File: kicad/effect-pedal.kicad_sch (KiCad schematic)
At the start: 83 parts, among them J1 NJ3FD-V, J10 USB_C_Receptacle_USB2.0_14P, J11 Conn_ST_STDC14, J2 NJ3FD-V, J3 Conn_01x08, J4 Conn_01x06, J5 Conn_01x06, J6 SOIC Bite Connector, J7 SOIC Bite Connector, J8 SOIC Bite Connector, J9 SOIC Bite Connector, Q1 NMOS, Q2 NMOS, SW1 RotaryEncoder_Switch, SW2 RotaryEncoder_Switch, SW3 RotaryEncoder_Switch, SW4 RotaryEncoder_Switch, SW5 SW_3PDT_x3, SW6 SW_SPDT, SW7 SW_Push, U1 STM32H723ZGTx, U2 PCM5102A, U3 USBLC6-2SC6, Y1 Crystal

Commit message: Finish part sourcing and start PCB layout
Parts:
- removed C27: 1u, Capacitor_SMD:C_0603_1608Metric, symbol Device:C
- removed C34: 10u, Capacitor_SMD:C_0603_1608Metric, symbol Device:C
- removed R3: 10k, Resistor_SMD:R_0603_1608Metric, symbol Device:R_US
- removed SW6: SW_SPDT, Button_Switch_SMD:SW_SPST_B3S-1100, symbol Switch:SW_SPDT
- removed TP5: TestPoint, TestPoint:TestPoint_Pad_2.0x2.0mm, symbol Connector:TestPoint
- added C28: 10u, Capacitor_SMD:C_0603_1608Metric, symbol Device:C
- added C33: 10n, Capacitor_SMD:C_0603_1608Metric, symbol Device:C
- added C8: 1u, Capacitor_SMD:C_0603_1608Metric, symbol Device:C
- added D3, D4: D_Schottky_Dual_Series_ACK_Split, Package_TO_SOT_SMD:TSOT-23, symbol Custom:D_Schottky_Dual_Series_ACK_Split_BAT
- added JP1: Jumper_2_Open, TestPoint:TestPoint_2Pads_Pitch2.54mm_Drill0.8mm, symbol Jumper:Jumper_2_Open
- added R1, R2: 1M, Resistor_SMD:R_0603_1608Metric, symbol Device:R_US
- added R15, R16: 100k, Resistor_SMD:R_0603_1608Metric, symbol Device:R_US
- added R17, R18: 100, Resistor_SMD:R_0603_1608Metric, symbol Device:R_US
- added R5: 10k, Resistor_SMD:R_0603_1608Metric, symbol Device:R_US
- J1, J2: value NJ3FD-V -> NJ6FD-H; symbol Connector_Audio:NJ3FD-V -> Connector_Audio:NJ6FD-V
- J10: footprint (none) -> Connector_USB:USB_C_Receptacle_GCT_USB4110; symbol Connector:USB_C_Receptacle_USB2.0_14P -> Connector:USB_C_Receptacle_USB2.0_16P; Part 2169900002 -> USB4110-GF-A
- J11: footprint Connector_TE-Connectivity:TE_MATE-N-LOK_1-770973-x_2x07_P4.14mm_Horizontal -> Connector_PinHeader_1.27mm:PinHeader_2x07_P1.27mm_Vertical_SMD; Part (none) -> FTSH-107-01-L-DV-K-A
- J3: footprint Connector_JST:JST_XH_S8B-XH-A_1x08_P2.50mm_Horizontal -> Connector_JST:JST_PH_S8B-PH-SM4-TB_1x08-1MP_P2.00mm_Horizontal; symbol Connector_Generic:Conn_01x08 -> Connector_Generic_MountingPin:Conn_01x08_MountingPin; Part Generic -> S8B-PH-SM4-TB
- J5: value Conn_01x06 -> Conn_01x09; footprint Connector_JST:JST_XH_S9B-XH-A_1x09_P2.50mm_Horizontal -> Connector_JST:JST_PH_S9B-PH-SM4-TB_1x09-1MP_P2.00mm_Horizontal; symbol Connector_Generic:Conn_01x09 -> Connector_Generic_MountingPin:Conn_01x09_MountingPin; Part Generic -> S9B-PH-SM4-TB
- J6, J7, J8, J9, TP1, TP2, TP3, TP4: now left out of the parts list
- R13: renamed from R11; value 3.3k -> 100k
- R14: renamed from R12; value 3.3k -> 100k
- SW1, SW2, SW3, SW4: footprint Rotary_Encoder:RotaryEncoder_Bourns_Vertical_PEC12R-3x17F-Sxxxx -> Bournes:RotaryEncoder_Bourns_Vertical_PEC12R-3x17F-Sxxxx; symbol Device:RotaryEncoder_Switch -> Device:RotaryEncoder_Switch_MP
- SW6: renamed from SW7; footprint Button_Switch_THT:SW_PUSH_6mm -> Button_Switch_SMD:SW_Push_1P1T_NO_E-Switch_TL3301NxxxxxG; Part (none) -> 1571563-6
- renumbered C9 to C10, C10 to C11, C11 to C12, C12 to C13, C13 to C14, C14 to C15, C15 to C16, C16 to C17, C17 to C18, C18 to C19, C22 to C20, C20 to C21, C19 to C22, C26 to C23, C21 to C24, C28 to C25, C23 to C26, C33 to C27, C25 to C29, C29 to C30, C30 to C31, C24 to C32, C31 to C34, C32 to C35, C8 to C9, JP1 to JP2, JP2 to JP3, JP3 to JP4, R9 to R10, R10 to R11, R8 to R12, R13 to R19, R14 to R20, R1 to R3, R2 to R4, R4 to R6, R5 to R7, R6 to R8, R7 to R9
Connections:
- net AUD_IN_L: now also C27.1; no longer U1.60 (PE9)
- net AUD_IN_L_AMP: no longer J6.3 (Pin_3)
- net AUD_IN_R: now also C28.1; no longer U1.46 (PB0)
- net AUD_IN_R_AMP: now also J6.7 (Pin_7); no longer J6.1 (Pin_1)
- net AUD_WET_R: now also R11.1; no longer R11.2
- net BOOT: now also JP1.2 (B), R5.1
- net DISPLAY_BL: now also J3.1 (Pin_1); no longer J3.8 (Pin_8)
- net DISPLAY_CS: now also J3.4 (Pin_4); no longer J3.5 (Pin_5)
- net DISPLAY_DATA: now also J3.6 (Pin_6); no longer J3.3 (Pin_3)
- net DISPLAY_DC: now also J3.3 (Pin_3); no longer J3.6 (Pin_6)
- net DISPLAY_RST: now also J3.2 (Pin_2); no longer J3.7 (Pin_7)
- net DISPLAY_SCK: now also J3.5 (Pin_5); no longer J3.4 (Pin_4)
- net GND: now also J1.S, J3.7 (Pin_7), J5.3 (Pin_3), R12.2, C33.1, C8.1, D3.1 (A), D4.1 (A), R1.2, R16.2, R2.2, R5.2; no longer J3.2 (Pin_2), R12.1
- net VCC: now also C30.1, C34.1, J3.8 (Pin_8), U1.6 (VBAT), JP1.1 (A); no longer C22.1, C24.1, C26.1, C29.1, J3.1 (Pin_1)
- net VDDA: now also C22.1, C24.1, C26.1, C29.1; no longer C31.1, C35.2
- net VREF+: now also C8.2, D3.2 (K), D4.2 (K), R15.1
- net at R13.2, R14.1: now also C27.2, R17.1; no longer C27.1, C32.2
- net at U2.7 (OUTR): now also R11.2; no longer R11.1
- removed net AUD_IN_GND: C27.2, J1.S, J5.3 (Pin_3), J6.7 (Pin_7)
- net SHIELD renamed GNDPWR
- net GNDPWR: now also J3.MP (MountPin), J5.MP (MountPin), R12.1, SW1.MP, SW2.MP, SW3.MP, SW4.MP; no longer R12.2
- new net: C31.1, C35.2, U2.18 (LDOO)
- new net: C28.2, R15.2, R16.1, R18.1
- new net AUD_IN_L_BIAS: C32.2, D3.3 (K), D3.3 (K), J6.3 (Pin_3), R17.2, U1.60 (PE9)
- new net AUD_IN_R_BIAS: C33.2, D4.3 (K), D4.3 (K), J6.1 (Pin_1), R18.2, U1.46 (PB0)
- new net AUD_N: J1.RN, J1.SN, J1.TN, J2.RN, J2.SN, J2.TN, R1.1, R2.1
- no-connect marks 2 -> 4
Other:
- note added: "Input DC Bias"
- note added: "Normalizing Ground"
- note removed: "Input Reference Ground"
- moved on the sheet: C10, C11, C12, C13, C14, C15, C16, C17, C18, C19, C20, C21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

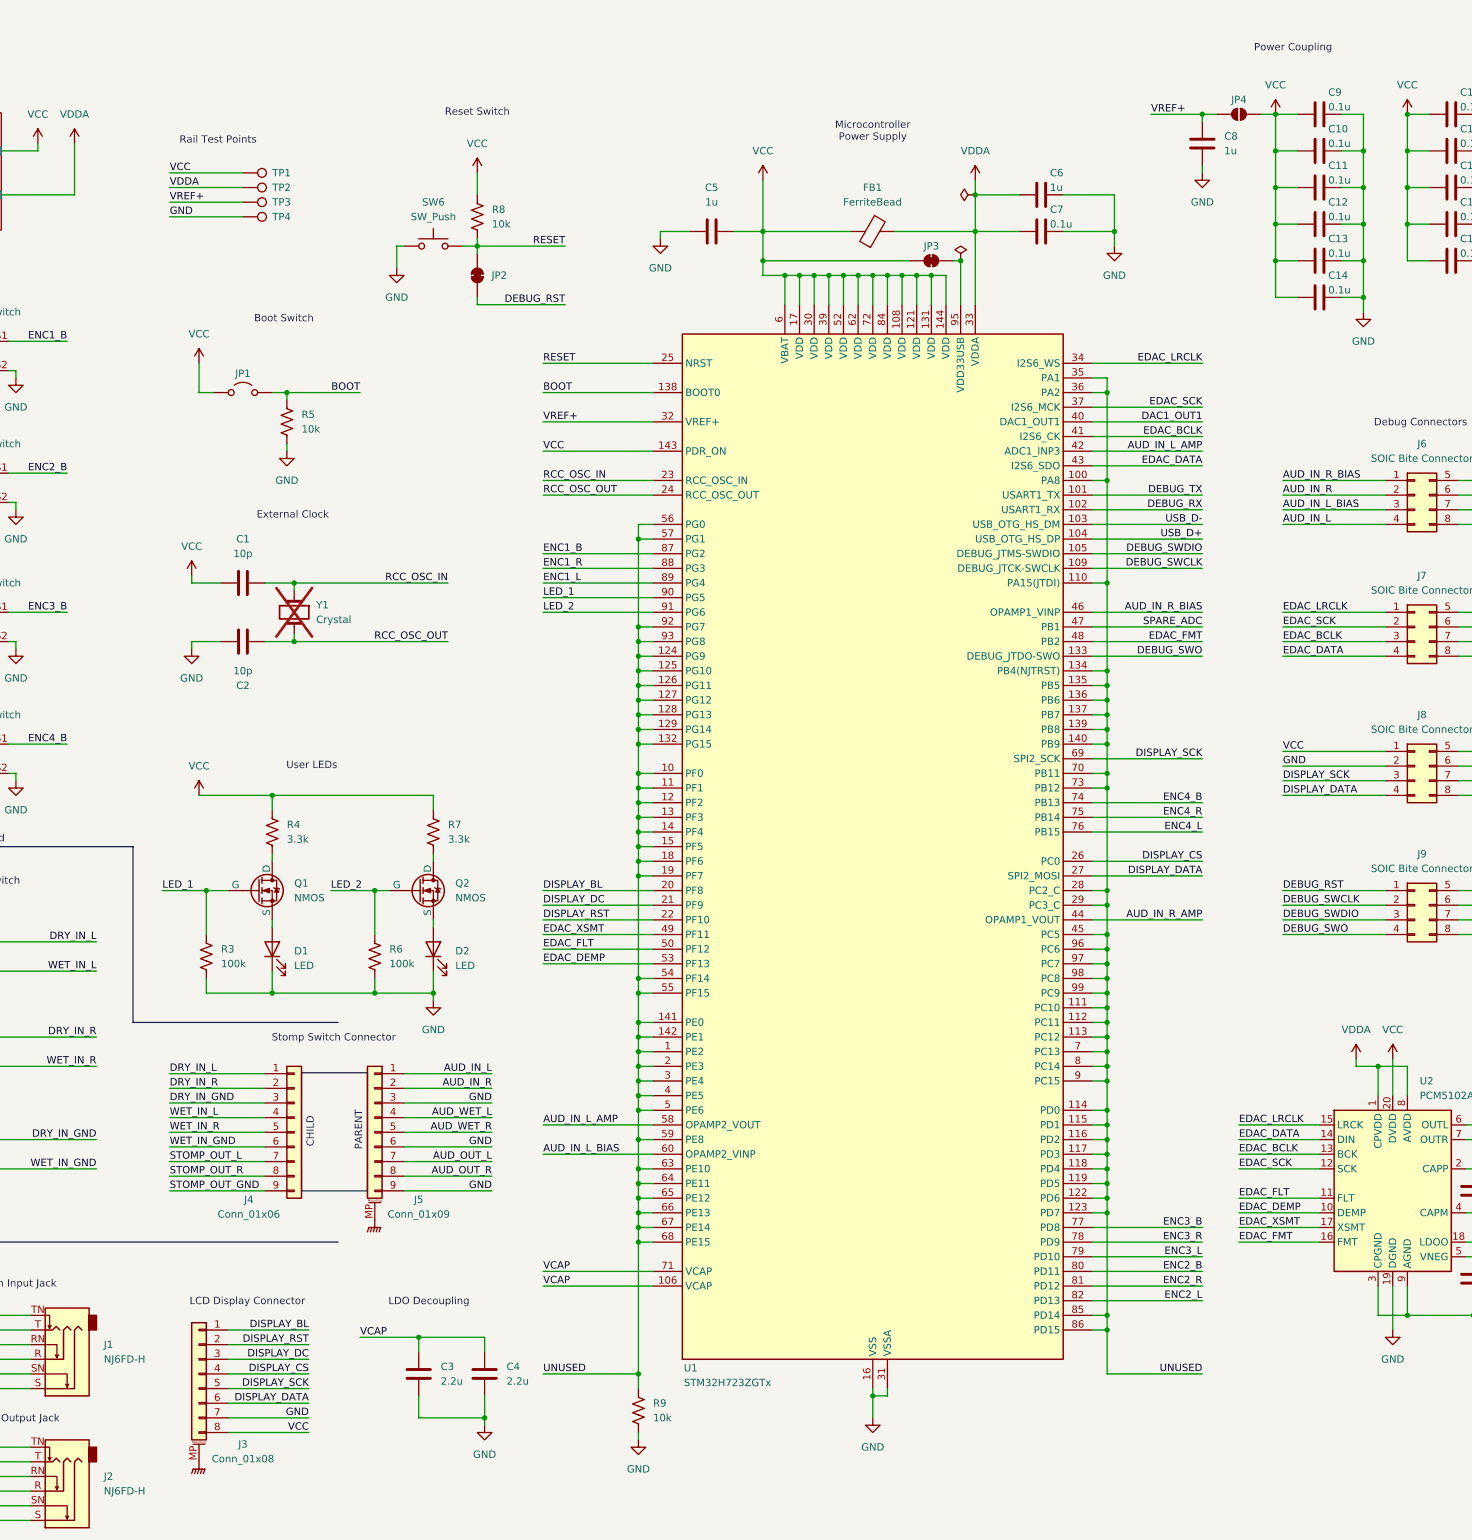
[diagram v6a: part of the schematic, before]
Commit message: Finish schematic
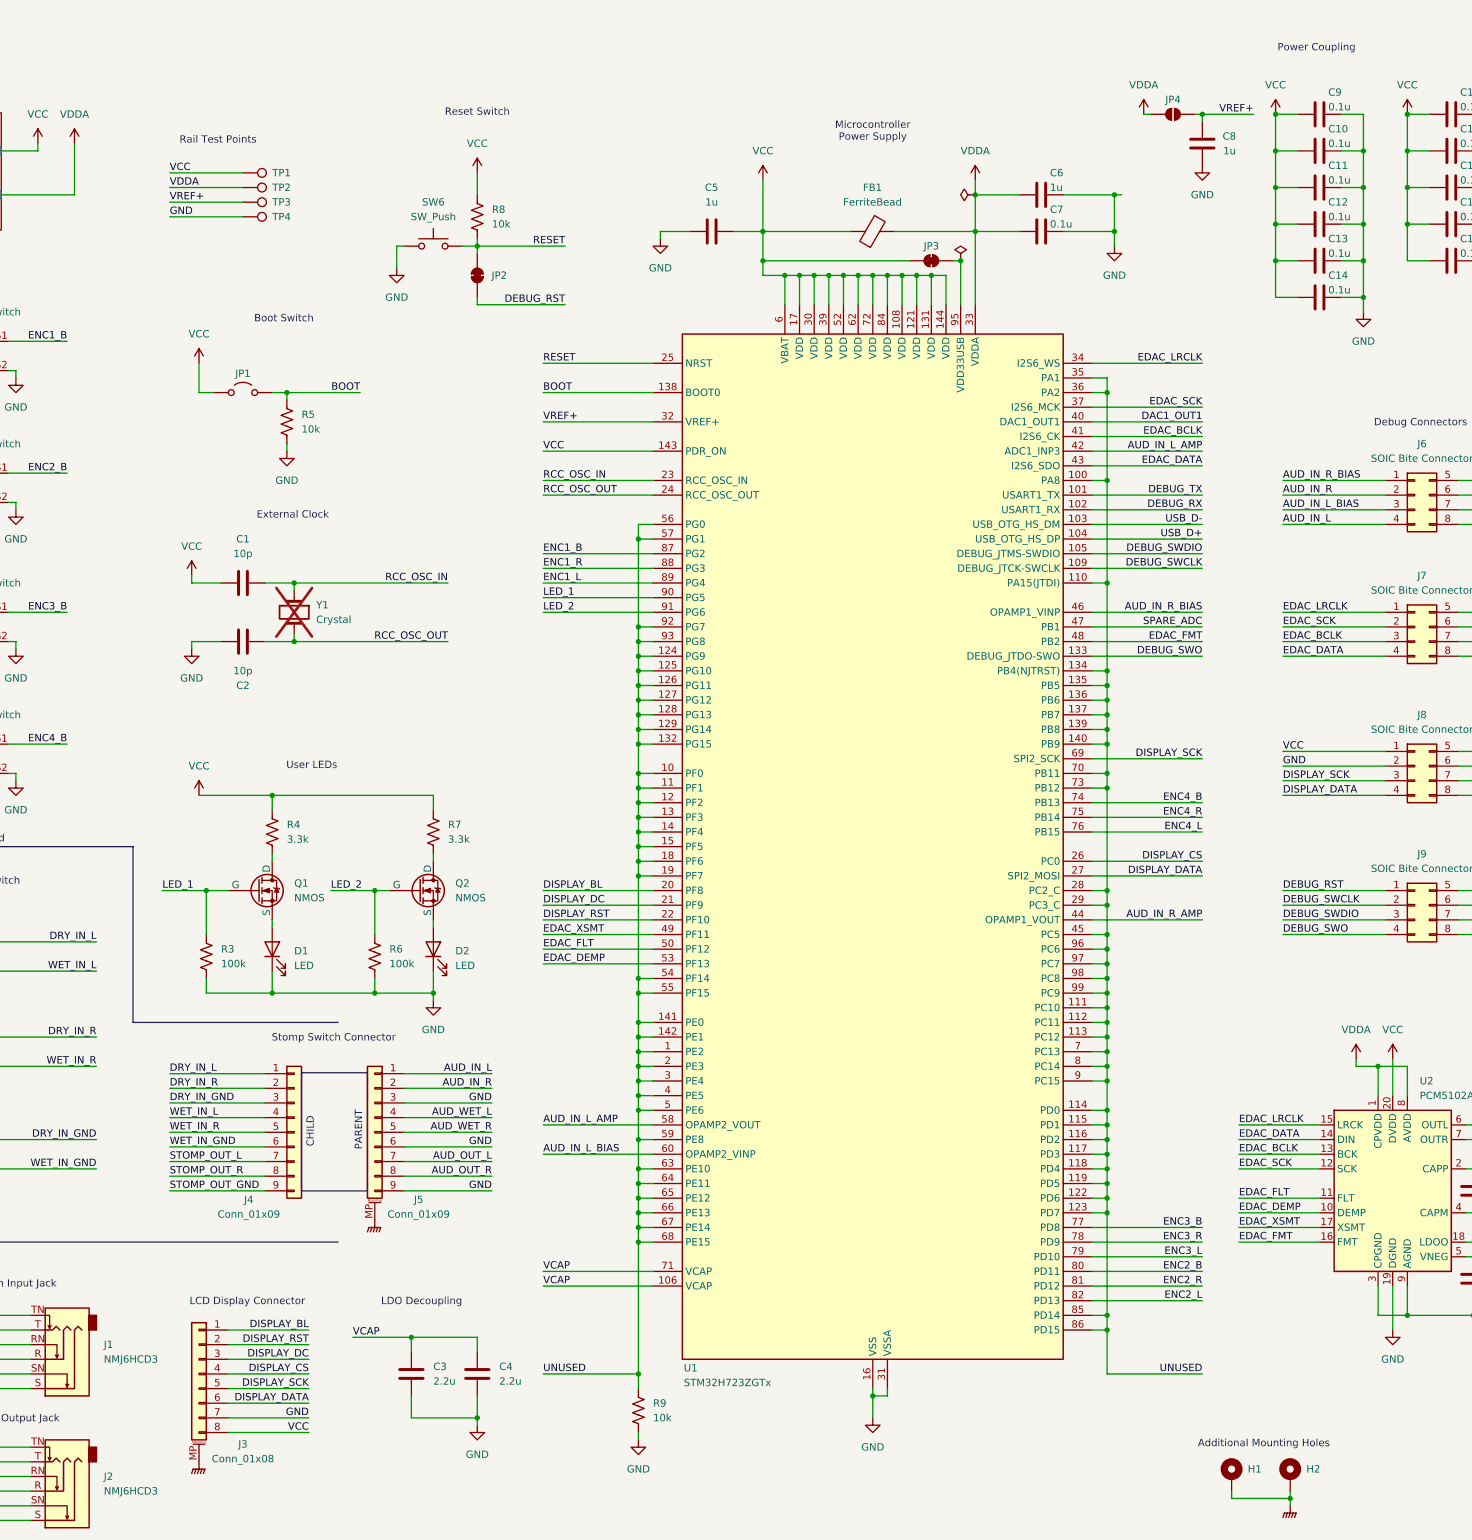
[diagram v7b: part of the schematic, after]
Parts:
- added H1, H2: MountingHole_Pad, MountingHole:MountingHole_2.2mm_M2_ISO7380_Pad, symbol Mechanical:MountingHole_Pad
- J1, J2: value NJ6FD-H -> NMJ6HCD3; footprint Connector_Audio:Jack_6.35mm_Neutrik_NMJ6HCD3_Horizontal -> Neutrik:Jack_6.35mm_Neutrik_NMJ6HCD3_Horizontal
- J10: footprint Connector_USB:USB_C_Receptacle_GCT_USB4110 -> Custom:USB_C_Receptacle_GCT_USB4110
- J11: footprint Connector_PinHeader_1.27mm:PinHeader_2x07_P1.27mm_Vertical_SMD -> Custom:STDC14_Connector; Part FTSH-107-01-L-DV-K-A -> 20021512-00014T1LF
- J3: footprint Connector_JST:JST_PH_S8B-PH-SM4-TB_1x08-1MP_P2.00mm_Horizontal -> Waveshare:Waveshare_2.4in_LCD; Part S8B-PH-SM4-TB -> 10129380-908001BLF
- J4: value Conn_01x06 -> Conn_01x09
- J5: footprint Connector_JST:JST_PH_S9B-PH-SM4-TB_1x09-1MP_P2.00mm_Horizontal -> Custom:JST_PH_S9B-PH-SM4-TB_1x09-1MP_P2.00mm_Horizontal
- SW1, SW2, SW3, SW4: Part PEC12R-4225F-S0024 -> PEC12R-4230F-S0024
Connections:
- net GNDPWR: now also H1.1, H2.1
- net VCC: no longer JP4.1 (A)
- net VDDA: now also JP4.1 (A)
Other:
- note added: "Additional Mounting Holes"
- moved on the sheet: C3, C4, C8, JP4

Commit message: Setup for production
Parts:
- C10, C11, C12, C13, C14, C15, C16, C17, C18, C19, C22, C24, C34, C35, C7, C9: Part GMK107BJ104MAHT -> CC0603KRX7R9BB104
- D1, D2: Part QBLP631-R -> LTST-C171EKT
- D3, D4: Part BAT54S_R1_00001 -> BAT54SFILM
- Q1, Q2: symbol Simulation_SPICE:NMOS -> Transistor_FET_Other:Q_NMOS_Depletion_DSG; Part AO3400 -> IRLML6344TRPBF
- SW6: Part 1571563-6 -> TS04-66-65-BK-260-SMT
- U1: Part STM32H723ZGT6TR -> STM32H723ZGT6
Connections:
- net LED_1: now also Q1.3 (G); no longer Q1.2 (G)
- net LED_2: now also Q2.3 (G); no longer Q2.2 (G)
- net at D1.2 (A): now also Q1.2 (S); no longer Q1.3 (S)
- net at D2.2 (A): now also Q2.2 (S); no longer Q2.3 (S)
